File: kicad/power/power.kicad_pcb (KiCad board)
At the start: 2 copper layers, 32.8 x 86.9 mm, 20 parts, among them J1 Conn_01x05, K1 SRD-12VDC-SL-C, P1 CONN_2, P2 CONN_3, P3 CONN_2, P4 CONN_2

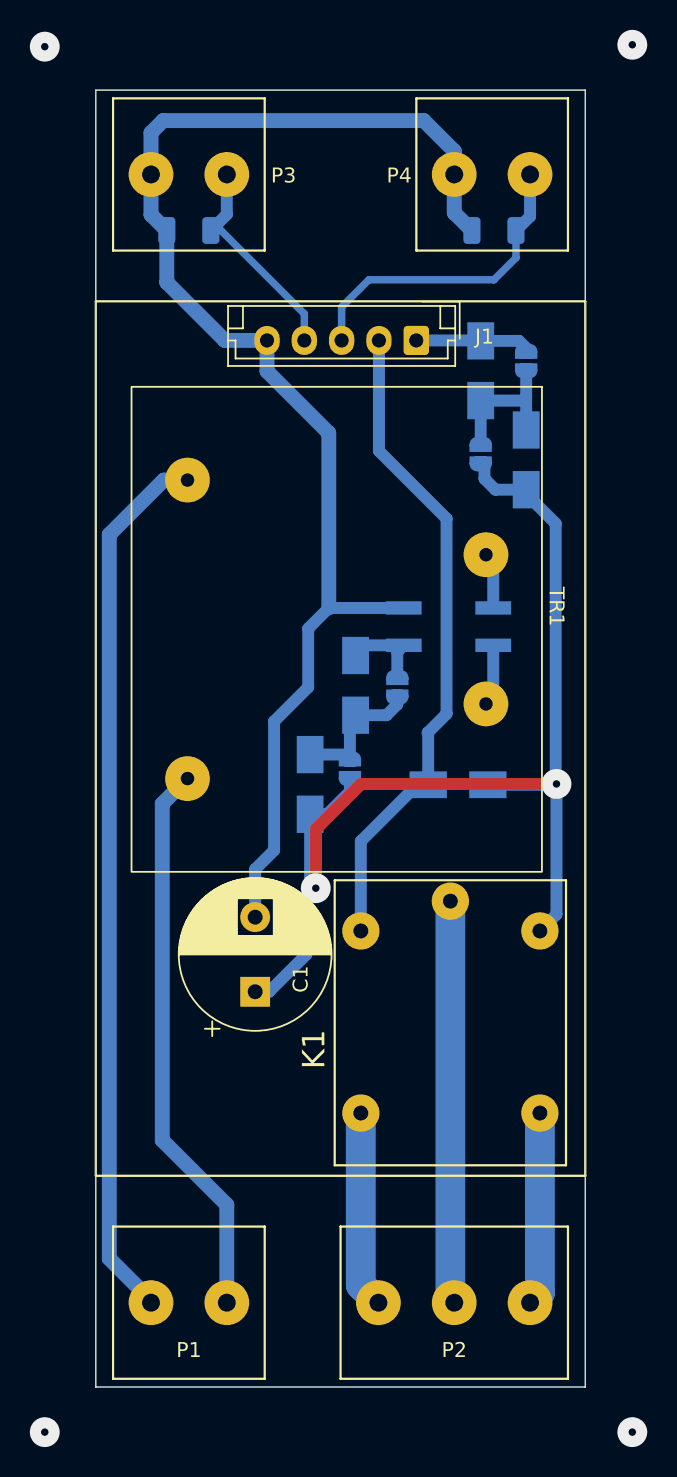
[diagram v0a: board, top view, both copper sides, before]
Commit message: На питании диоды замкнул перемычками
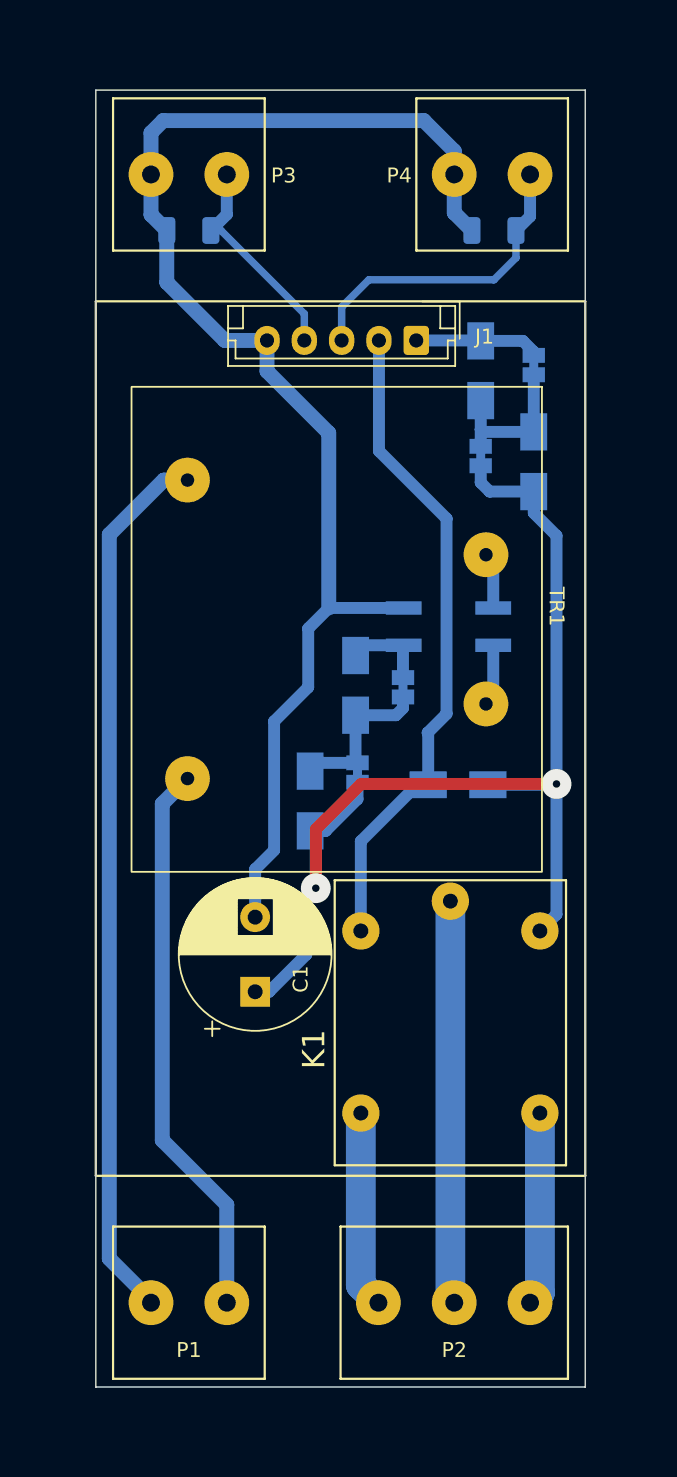
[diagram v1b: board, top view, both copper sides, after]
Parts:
- JP1, JP2, JP3, JP4: value SolderJumper_2_Open -> SolderJumper_2_Bridged; footprint Jumper:SolderJumper-2_P1.3mm_Open_RoundedPad1.0x1.5mm -> Jumper:SolderJumper-2_P1.3mm_Bridged_Pad1.0x1.5mm
- moved D3 1.11 mm to (248.6, 71.9)
- moved JP4 0.57 mm to (263.5, 42.7)
- moved JP2 0.57 mm to (251.7, 70.0)
- moved D4 0.52 mm to (263.5, 49.2)
- moved JP1 0.38 mm to (254.8, 64.3)
- moved JP3 0.13 mm to (260.0, 48.8)
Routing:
- net Net-(D2-Pad1): track 9.48 -> 10.8 mm
- net Net-(D5-Pad1): track 7.80 -> 8.43 mm
- net (no net): vias 4 -> 0
